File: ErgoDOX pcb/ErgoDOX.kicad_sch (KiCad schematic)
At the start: 91 parts, among them J1 USB_RH, J10 USB VCC, J2 3.5mm, J3 JMP, J4 JMP, J5 BT_JMP, J6 EN_JMP, J7 PROG, J8 JTAG, J9 USB GND, SW0:10 SW0:3, SW0:11 SW0:2, SW0:12 SW0:1, SW0:7 SW0:6, SW0:8 SW0:5, SW0:9 SW0:4, SW1:10 SW1:3, SW1:11 SW1:2, SW1:12 SW1:1, SW1:13 SW1:0, SW1:9 SW1:4, SW2:10 SW2:3, SW2:11 SW2:2, SW2:12 SW2:1, SW2:13 SW2:0, SW2:7 SW2:6, SW2:8 SW2:5, SW2:9 SW2:4, SW3:10 SW3:3, SW3:11 SW3:2, SW3:12 SW3:1, SW3:13 SW3:0, SW3:8 SW3:5, SW3:9 SW3:4, SW4:10 SW4:3, SW4:11 SW4:2, SW4:12 SW4:1, SW4:13 SW4:0, SW4:7 SW4:6, SW4:8 SW4:5, SW4:9 SW4:4, SW5:10 SW5:3, SW5:11 SW5:2, SW5:12 SW5:1, SW5:13 SW5:0, SW5:7 SW5:6, SW5:8 SW5:5, SW5:9 SW5:4, U1 LM337_SOT223

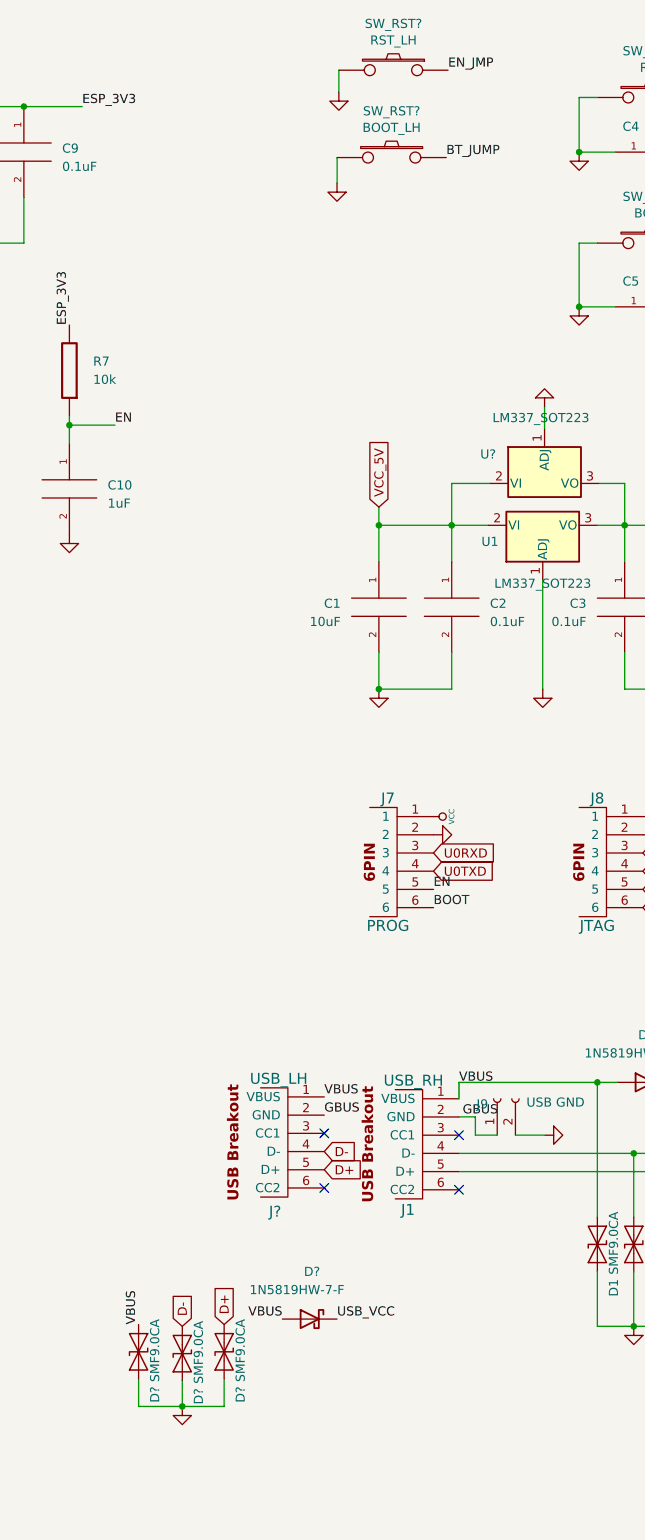
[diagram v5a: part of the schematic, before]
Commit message: Add silkscreen notes and logo
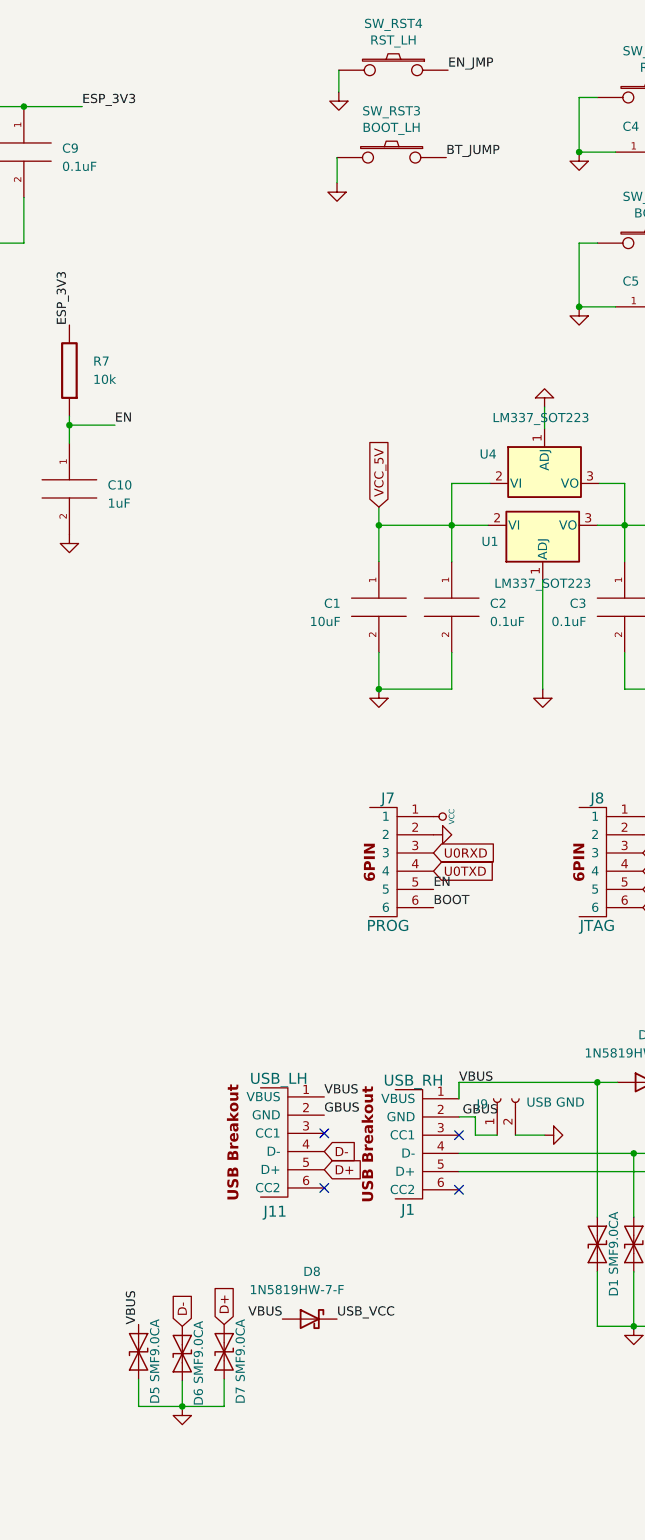
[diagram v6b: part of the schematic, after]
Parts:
- gave numbers to parts that had none: 8
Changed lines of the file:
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@@
   (symbol (lib_id "Diode:ESD9B3.3ST5G") (at 303.022 201.676 270) (mirror x) (unit 1)
     (in_bom yes) (on_board yes)
-    (property "Reference" "D?" (id 0) (at 305.308 206.502 0)
+    (property "Reference" "D5" (id 0) (at 305.308 206.502 0)
       (effects (font (size 1.27 1.27)) (justify right))
     )
@@
   (symbol (lib_id "component:GND") (at 309.118 210.566 0) (mirror y) (unit 1)
     (in_bom yes) (on_board yes)
-    (property "Reference" "#PWR?" (id 0) (at 309.118 210.566 0)
+    (property "Reference" "#PWR015" (id 0) (at 309.118 210.566 0)
       (effects (font (size 0.762 0.762)) hide)
     )
@@
   (symbol (lib_id "component:SWITCH_PUSH") (at 338.582 22.86 0) (mirror y) (unit 1)
     (in_bom yes) (on_board yes)
-    (property "Reference" "SW_RST?" (id 0) (at 338.582 16.383 0))
+    (property "Reference" "SW_RST4" (id 0) (at 338.582 16.383 0))
     (property "Value" "RST_LH" (id 1) (at 338.582 18.6944 0))
     (property "Footprint" "Button_Switch_SMD:SW_SPST_B3U-1000P" (id 2) (at 338.582 22.86 0)
@@
   (symbol (lib_name "6PIN_1") (lib_id "component:6PIN") (at 323.85 172.466 0) (unit 1)
     (in_bom yes) (on_board yes)
-    (property "Reference" "J?" (id 0) (at 322.072 182.118 0)
+    (property "Reference" "J11" (id 0) (at 322.072 182.118 0)
       (effects (font (size 1.524 1.524)))
     )
@@
   (symbol (lib_id "component:GND") (at 330.962 27.178 0) (mirror y) (unit 1)
     (in_bom yes) (on_board yes)
-    (property "Reference" "#PWR?" (id 0) (at 330.962 27.178 0)
+    (property "Reference" "#PWR022" (id 0) (at 330.962 27.178 0)
       (effects (font (size 0.762 0.762)) hide)
     )
@@
   (symbol (lib_id "Diode:1N5819") (at 326.898 197.104 0) (mirror y) (unit 1)
     (in_bom yes) (on_board yes)
-    (property "Reference" "D?" (id 0) (at 327.2155 190.5 0))
+    (property "Reference" "D8" (id 0) (at 327.2155 190.5 0))
     (property "Value" "1N5819HW-7-F" (id 1) (at 325.12 193.04 0))
     (property "Footprint" "Diode_SMD:D_SOD-123" (id 2) (at 326.898 201.549 0)
@@
   (symbol (lib_id "Regulator_Linear:LM337_SOT223") (at 359.664 80.518 0) (unit 1)
     (in_bom yes) (on_board yes)
-    (property "Reference" "U?" (id 0) (at 351.79 76.454 0))
+    (property "Reference" "U4" (id 0) (at 351.79 76.454 0))
     (property "Value" "LM337_SOT223" (id 1) (at 359.156 71.374 0))
     (property "Footprint" "Package_TO_SOT_SMD:SOT-223-3_TabPin2" (id 2) (at 359.664 85.598 0)
@@
   (symbol (lib_id "Diode:ESD9B3.3ST5G") (at 309.118 201.93 270) (mirror x) (unit 1)
     (in_bom yes) (on_board yes)
-    (property "Reference" "D?" (id 0) (at 311.404 206.756 0)
+    (property "Reference" "D6" (id 0) (at 311.404 206.756 0)
       (effects (font (size 1.27 1.27)) (justify right))
     )
@@
   (symbol (lib_id "component:GND") (at 359.664 68.58 0) (mirror x) (unit 1)
     (in_bom yes) (on_board yes)
-    (property "Reference" "#PWR?" (id 0) (at 359.664 68.58 0)
+    (property "Reference" "#PWR028" (id 0) (at 359.664 68.58 0)
       (effects (font (size 0.762 0.762)) hide)
     )
@@
   (symbol (lib_id "Diode:ESD9B3.3ST5G") (at 314.96 201.676 270) (mirror x) (unit 1)
     (in_bom yes) (on_board yes)
-    (property "Reference" "D?" (id 0) (at 317.246 206.502 0)
+    (property "Reference" "D7" (id 0) (at 317.246 206.502 0)
       (effects (font (size 1.27 1.27)) (justify right))
     )
@@
   (symbol (lib_id "component:GND") (at 330.708 39.878 0) (mirror y) (unit 1)
     (in_bom yes) (on_board yes)
-    (property "Reference" "#PWR?" (id 0) (at 330.708 39.878 0)
+    (property "Reference" "#PWR017" (id 0) (at 330.708 39.878 0)
       (effects (font (size 0.762 0.762)) hide)
     )
@@
   (symbol (lib_id "component:SWITCH_PUSH") (at 338.328 35.052 0) (mirror y) (unit 1)
     (in_bom yes) (on_board yes)
-    (property "Reference" "SW_RST?" (id 0) (at 338.328 28.575 0))
+    (property "Reference" "SW_RST3" (id 0) (at 338.328 28.575 0))
     (property "Value" "BOOT_LH" (id 1) (at 338.328 30.8864 0))
     (property "Footprint" "Button_Switch_SMD:SW_SPST_B3U-1000P" (id 2) (at 338.328 35.052 0)
@@
       (reference "#PWR014") (unit 1) (value "GND") (footprint "")
     )
+    (path "/1179e5fb-c6eb-49e9-9332-90a9b0a82bf9"
+      (reference "#PWR015") (unit 1) (value "GND") (footprint "")
+    )
     (path "/2e9c0f6e-df45-4464-ac85-74d0f13ba3da"
       (reference "#PWR016") (unit 1) (value "VCC") (footprint "")
     )
+    (path "/ac4dc690-0176-4983-8d5d-f9a95afb317b"
+      (reference "#PWR017") (unit 1) (value "GND") (footprint "")
+    )
     (path "/439ab8d7-c5d1-4fcd-a7bd-9b819c4a780a"
       (reference "#PWR018") (unit 1) (value "GND") (footprint "")
@@
       (reference "#PWR021") (unit 1) (value "GND") (footprint "")
     )
+    (path "/2f382bc0-533a-4991-9e07-bc1bd10ad5eb"
+      (reference "#PWR022") (unit 1) (value "GND") (footprint "")
+    )
     (path "/f177451e-5403-4067-9c12-cc7cc4c38353"
       (reference "#PWR023") (unit 1) (value "GND") (footprint "")
@@
       (reference "#PWR027") (unit 1) (value "GND") (footprint "")
     )
+    (path "/9eddb616-83cc-4c20-9381-79aa48a47aae"
+      (reference "#PWR028") (unit 1) (value "GND") (footprint "")
+    )
     (path "/18ff92bb-5363-4719-a220-bfe48d0b15ea/cabe4a87-f007-4763-92c6-1c89d9b49a9f"
       (reference "#PWR031") (unit 1) (value "GND") (footprint "")
@@
       (reference "#PWR035") (unit 1) (value "GND") (footprint "")
     )
-    (path "/1179e5fb-c6eb-49e9-9332-90a9b0a82bf9"
-      (reference "#PWR?") (unit 1) (value "GND") (footprint "")
-    )
-    (path "/2f382bc0-533a-4991-9e07-bc1bd10ad5eb"
-      (reference "#PWR?") (unit 1) (value "GND") (footprint "")
-    )
-    (path "/9eddb616-83cc-4c20-9381-79aa48a47aae"
-      (reference "#PWR?") (unit 1) (value "GND") (footprint "")
-    )
-    (path "/ac4dc690-0176-4983-8d5d-f9a95afb317b"
-      (reference "#PWR?") (unit 1) (value "GND") (footprint "")
-    )
     (path "/b93eb7b0-47b0-4f54-9ee1-5cac4e593e1a"
       (reference "C1") (unit 1) (value "10uF") (footprint "Capacitor_THT:C_Disc_D5.0mm_W2.5mm_P5.00mm")
@@
     )
     (path "/0a81c4f0-f8fe-4eb6-969c-1d837b9904f2"
-      (reference "D?") (unit 1) (value "SMF9.0CA") (footprint "Diode_SMD:D_SOD-123")
+      (reference "D5") (unit 1) (value "SMF9.0CA") (footprint "Diode_SMD:D_SOD-123")
+    )
+    (path "/81a4f26f-3ba1-4f87-8263-be9a27aabfc5"
+      (reference "D6") (unit 1) (value "SMF9.0CA") (footprint "Diode_SMD:D_SOD-123")
+    )
+    (path "/a67cad06-d61f-48b8-a5b0-43e3655248cb"
+      (reference "D7") (unit 1) (value "SMF9.0CA") (footprint "Diode_SMD:D_SOD-123")
     )
     (path "/7363d8c3-059b-4f1c-bb6e-d524dd3d7421"
-      (reference "D?") (unit 1) (value "1N5819HW-7-F") (footprint "Diode_SMD:D_SOD-123")
-    )
-    (path "/81a4f26f-3ba1-4f87-8263-be9a27aabfc5"
-      (reference "D?") (unit 1) (value "SMF9.0CA") (footprint "Diode_SMD:D_SOD-123")
-    )
-    (path "/a67cad06-d61f-48b8-a5b0-43e3655248cb"
-      (reference "D?") (unit 1) (value "SMF9.0CA") (footprint "Diode_SMD:D_SOD-123")
+      (reference "D8") (unit 1) (value "1N5819HW-7-F") (footprint "Diode_SMD:D_SOD-123")
     )
     (path "/00000000-0000-0000-0000-00004ec43592"
@@
     )
     (path "/2b883784-3d8d-4546-bd1e-18b4f3cd5953"
-      (reference "J?") (unit 1) (value "USB_LH") (footprint "ErgoDOX pcb:SF USB-C Breakout")
+      (reference "J11") (unit 1) (value "USB_LH") (footprint "ErgoDOX pcb:SF USB-C Breakout")
     )
     (path "/00000000-0000-0000-0000-00004f64e802"
@@
       (reference "SW_RST2") (unit 1) (value "BOOT") (footprint "Button_Switch_SMD:SW_SPST_B3U-1000P")
     )
+    (path "/bf08161f-7a50-49f2-8435-ba34603e2599"
+      (reference "SW_RST3") (unit 1) (value "BOOT_LH") (footprint "Button_Switch_SMD:SW_SPST_B3U-1000P")
+    )
     (path "/245e9ccb-5f96-41af-a010-f6ea79a3907f"
-      (reference "SW_RST?") (unit 1) (value "RST_LH") (footprint "Button_Switch_SMD:SW_SPST_B3U-1000P")
-    )
-    (path "/bf08161f-7a50-49f2-8435-ba34603e2599"
-      (reference "SW_RST?") (unit 1) (value "BOOT_LH") (footprint "Button_Switch_SMD:SW_SPST_B3U-1000P")
+      (reference "SW_RST4") (unit 1) (value "RST_LH") (footprint "Button_Switch_SMD:SW_SPST_B3U-1000P")
     )
     (path "/00000000-0000-0000-0000-00004ffe197c"
@@
     )
     (path "/7db6ad57-89fc-470a-be55-bec89ac4e493"
-      (reference "U?") (unit 1) (value "LM337_SOT223") (footprint "Package_TO_SOT_SMD:SOT-223-3_TabPin2")
-    )
-  )
+      (reference "U4") (unit 1) (value "LM337_SOT223") (footprint "Package_TO_SOT_SMD:SOT-223-3_TabPin2")
+    )
+  )
